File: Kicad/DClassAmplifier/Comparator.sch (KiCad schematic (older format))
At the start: 5 parts

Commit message: Finish off Main Part of Schematic
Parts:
- U? (x3): footprint (none) -> Package_SO:SO-14_3.9x8.65mm_P1.27mm
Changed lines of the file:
@@
 $Descr A4 11693 8268
 encoding utf-8
-Sheet 7 9
+Sheet 3 7
 Title ""
 Date ""
@@
 F 0 "U?" H 5150 3242 50  0000 C CNN
 F 1 "LM319" H 5150 3151 50  0000 C CNN
-F 2 "" H 5150 2875 50  0001 C CNN
+F 2 "Package_SO:SO-14_3.9x8.65mm_P1.27mm" H 5150 2875 50  0001 C CNN
 F 3 "http://www.ti.com/lit/ds/symlink/lm319-n.pdf" H 5150 2875 50  0001 C CNN
 	1    5150 2875
@@
 F 0 "U?" H 5125 3792 50  0000 C CNN
 F 1 "LM319" H 5125 3701 50  0000 C CNN
-F 2 "" H 5125 3425 50  0001 C CNN
+F 2 "Package_SO:SO-14_3.9x8.65mm_P1.27mm" H 5125 3425 50  0001 C CNN
 F 3 "http://www.ti.com/lit/ds/symlink/lm319-n.pdf" H 5125 3425 50  0001 C CNN
 	2    5125 3425
@@
 F 0 "U?" H 5183 4546 50  0000 L CNN
 F 1 "LM319" H 5183 4455 50  0000 L CNN
-F 2 "" H 5225 4500 50  0001 C CNN
+F 2 "Package_SO:SO-14_3.9x8.65mm_P1.27mm" H 5225 4500 50  0001 C CNN
 F 3 "http://www.ti.com/lit/ds/symlink/lm319-n.pdf" H 5225 4500 50  0001 C CNN
 	3    5225 4500

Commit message: updates to schematic
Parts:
- added J2: Conn_01x03, symbol Connector_Generic:Conn_01x03
- R5, R6: renamed from R?; footprint (none) -> Resistor_SMD:R_0603_1608Metric_Pad0.98x0.95mm_HandSolder
- gave numbers to parts that had none: 1
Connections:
- net GND: now also J2.3 (Pin_3)
- net INV_PWM_OUT: now also J2.2 (Pin_2)
- net PWM_OUT: now also J2.1 (Pin_1)
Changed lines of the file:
@@
 $EndDescr
 $Comp
-L Comparator:LM319 U?
+L Comparator:LM319 U1
 U 1 1 61116116
 P 5150 2875
-F 0 "U?" H 5150 3242 50  0000 C CNN
+F 0 "U1" H 5150 3242 50  0000 C CNN
 F 1 "LM319" H 5150 3151 50  0000 C CNN
 F 2 "Package_SO:SO-14_3.9x8.65mm_P1.27mm" H 5150 2875 50  0001 C CNN
@@
 $EndComp
 $Comp
-L Comparator:LM319 U?
+L Comparator:LM319 U1
 U 2 1 6111611C
 P 5125 3425
-F 0 "U?" H 5125 3792 50  0000 C CNN
+F 0 "U1" H 5125 3792 50  0000 C CNN
 F 1 "LM319" H 5125 3701 50  0000 C CNN
 F 2 "Package_SO:SO-14_3.9x8.65mm_P1.27mm" H 5125 3425 50  0001 C CNN
@@
 $EndComp
 $Comp
-L Comparator:LM319 U?
+L Comparator:LM319 U1
 U 3 1 61116122
 P 5225 4500
-F 0 "U?" H 5183 4546 50  0000 L CNN
+F 0 "U1" H 5183 4546 50  0000 L CNN
 F 1 "LM319" H 5183 4455 50  0000 L CNN
 F 2 "Package_SO:SO-14_3.9x8.65mm_P1.27mm" H 5225 4500 50  0001 C CNN
@@
 	1    0    0    -1
 $EndComp
-Wire Wire Line
-	6275 2875 5825 2875
 Wire Wire Line
 	4850 2975 4775 2975
@@
 	4675 3525 4825 3525
 $Comp
-L power:GND #PWR?
+L power:GND #PWR0106
 U 1 1 61116132
 P 5150 3175
-F 0 "#PWR?" H 5150 2925 50  0001 C CNN
+F 0 "#PWR0106" H 5150 2925 50  0001 C CNN
 F 1 "GND" H 5155 3002 50  0000 C CNN
 F 2 "" H 5150 3175 50  0001 C CNN
@@
 $EndComp
 $Comp
-L power:GND #PWR?
+L power:GND #PWR0107
 U 1 1 61116138
 P 5125 3725
-F 0 "#PWR?" H 5125 3475 50  0001 C CNN
+F 0 "#PWR0107" H 5125 3475 50  0001 C CNN
 F 1 "GND" H 5130 3552 50  0000 C CNN
 F 2 "" H 5125 3725 50  0001 C CNN
@@
 $EndComp
 $Comp
-L power:GND #PWR?
+L power:GND #PWR0108
 U 1 1 6111613E
 P 5125 4800
-F 0 "#PWR?" H 5125 4550 50  0001 C CNN
+F 0 "#PWR0108" H 5125 4550 50  0001 C CNN
 F 1 "GND" H 5130 4627 50  0000 C CNN
 F 2 "" H 5125 4800 50  0001 C CNN
@@
 $EndComp
 $Comp
-L power:VCC #PWR?
+L power:VCC #PWR0109
 U 1 1 61116144
 P 5125 4200
-F 0 "#PWR?" H 5125 4050 50  0001 C CNN
+F 0 "#PWR0109" H 5125 4050 50  0001 C CNN
 F 1 "VCC" H 5140 4373 50  0000 C CNN
 F 2 "" H 5125 4200 50  0001 C CNN
@@
 	1    0    0    -1
 $EndComp
-Text HLabel 6275 2875 2    50   Output ~ 0
-PWM_OUT
-Text HLabel 6275 3425 2    50   Output ~ 0
+Text HLabel 7875 3075 2    50   Output ~ 0
 INV_PWM_OUT
 Text HLabel 4350 2975 0    50   Input ~ 0
@@
 	5425 3425 5825 3425
 $Comp
-L Device:R_Small R?
+L Device:R_Small R5
 U 1 1 61119BD5
 P 5825 2700
-F 0 "R?" H 5884 2746 50  0000 L CNN
+F 0 "R5" H 5884 2746 50  0000 L CNN
 F 1 "10k" H 5884 2655 50  0000 L CNN
-F 2 "" H 5825 2700 50  0001 C CNN
+F 2 "Resistor_SMD:R_0603_1608Metric_Pad0.98x0.95mm_HandSolder" H 5825 2700 50  0001 C CNN
 F 3 "~" H 5825 2700 50  0001 C CNN
 	1    5825 2700
@@
 $EndComp
 $Comp
-L Device:R_Small R?
+L Device:R_Small R6
 U 1 1 6111A188
 P 5825 3250
-F 0 "R?" H 5884 3296 50  0000 L CNN
+F 0 "R6" H 5884 3296 50  0000 L CNN
 F 1 "10k" H 5884 3205 50  0000 L CNN
-F 2 "" H 5825 3250 50  0001 C CNN
+F 2 "Resistor_SMD:R_0603_1608Metric_Pad0.98x0.95mm_HandSolder" H 5825 3250 50  0001 C CNN
 F 3 "~" H 5825 3250 50  0001 C CNN
 	1    5825 3250
@@
 $EndComp
 $Comp
-L power:VCC #PWR?
+L power:VCC #PWR0110
 U 1 1 6111A8CA
 P 5825 2500
-F 0 "#PWR?" H 5825 2350 50  0001 C CNN
+F 0 "#PWR0110" H 5825 2350 50  0001 C CNN
 F 1 "VCC" H 5840 2673 50  0000 C CNN
 F 2 "" H 5825 2500 50  0001 C CNN
@@
 $EndComp
 $Comp
-L power:VCC #PWR?
+L power:VCC #PWR0111
 U 1 1 6111AE94
 P 5825 3100
-F 0 "#PWR?" H 5825 2950 50  0001 C CNN
+F 0 "#PWR0111" H 5825 2950 50  0001 C CNN
 F 1 "VCC" H 5840 3273 50  0000 C CNN
 F 2 "" H 5825 3100 50  0001 C CNN
@@
 Wire Wire Line
 	5825 2875 5825 2800
-Connection ~ 5825 2875
 Wire Wire Line
 	5825 2875 5450 2875
@@
 	4775 2975 4350 2975
 Connection ~ 4775 2975
+$Comp
+L Connector_Generic:Conn_01x03 J2
+U 1 1 611080B2
+P 7675 3075
+F 0 "J2" H 7755 3117 50  0000 L CNN
+F 1 "Conn_01x03" H 7755 3026 50  0000 L CNN
+F 2 "" H 7675 3075 50  0001 C CNN
+F 3 "~" H 7675 3075 50  0001 C CNN
+	1    7675 3075
+	-1   0    0    -1
+$EndComp
+Text HLabel 7875 2975 2    50   Output ~ 0
+PWM_OUT
+Connection ~ 5825 2875
+Wire Wire Line
+	6275 2875 5825 2875
+$Comp
+L power:GND #PWR0112
+U 1 1 6110885B
+P 7875 3175
+F 0 "#PWR0112" H 7875 2925 50  0001 C CNN
+F 1 "GND" H 7880 3002 50  0000 C CNN
+F 2 "" H 7875 3175 50  0001 C CNN
+F 3 "" H 7875 3175 50  0001 C CNN
+	1    7875 3175
+	-1   0    0    -1
+$EndComp
+Text Label 7875 2975 0    50   ~ 0
+PWM_OUT
+Text Label 7875 3075 0    50   ~ 0
+INV_PWM_OUT
+Text Label 6275 2875 0    50   ~ 0
+PWM_OUT
+Text Label 6275 3425 0    50   ~ 0
+INV_PWM_OUT
 $EndSCHEMATC

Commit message: Added footprints to schematic
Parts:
- J2: footprint (none) -> Connector_PinSocket_2.54mm:PinSocket_1x03_P2.54mm_Vertical
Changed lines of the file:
@@
 F 0 "J2" H 7755 3117 50  0000 L CNN
 F 1 "Conn_01x03" H 7755 3026 50  0000 L CNN
-F 2 "" H 7675 3075 50  0001 C CNN
+F 2 "Connector_PinSocket_2.54mm:PinSocket_1x03_P2.54mm_Vertical" H 7675 3075 50  0001 C CNN
 F 3 "~" H 7675 3075 50  0001 C CNN
 	1    7675 3075

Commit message: Update Terminal Block Footprints
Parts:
- J2: footprint Connector_PinSocket_2.54mm:PinSocket_1x03_P2.54mm_Vertical -> TerminalBlock:TerminalBlock_bornier-3_P5.08mm
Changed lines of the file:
@@
 F 0 "J2" H 7755 3117 50  0000 L CNN
 F 1 "Conn_01x03" H 7755 3026 50  0000 L CNN
-F 2 "Connector_PinSocket_2.54mm:PinSocket_1x03_P2.54mm_Vertical" H 7675 3075 50  0001 C CNN
+F 2 "TerminalBlock:TerminalBlock_bornier-3_P5.08mm" H 7675 3075 50  0001 C CNN
 F 3 "~" H 7675 3075 50  0001 C CNN
 	1    7675 3075

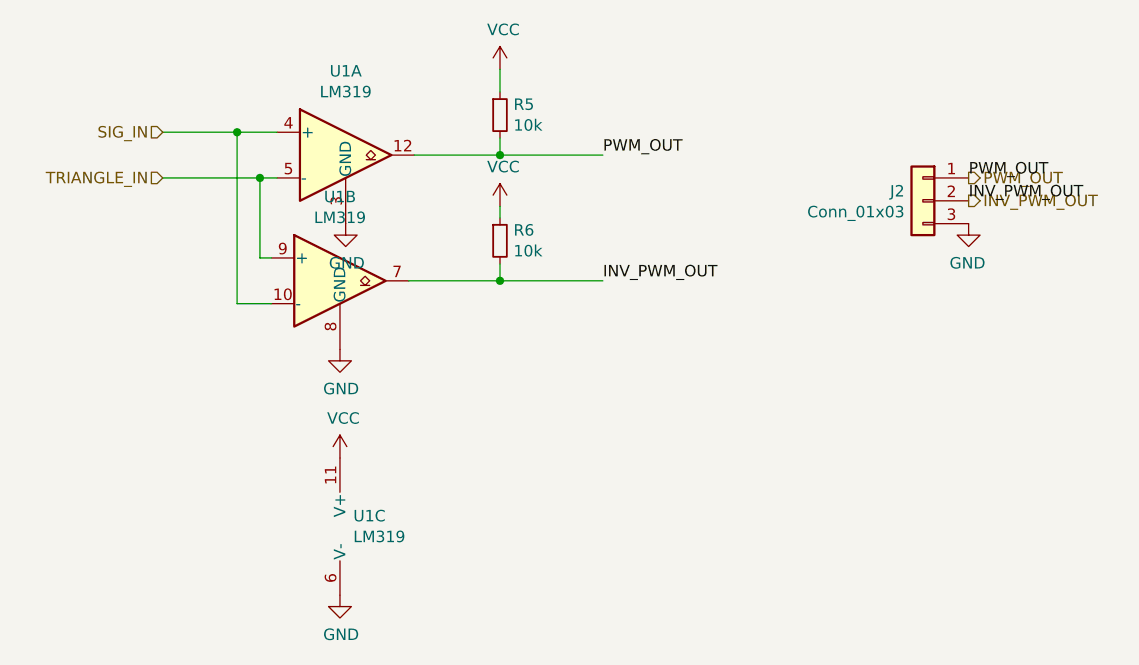
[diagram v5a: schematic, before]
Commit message: Add Test Points
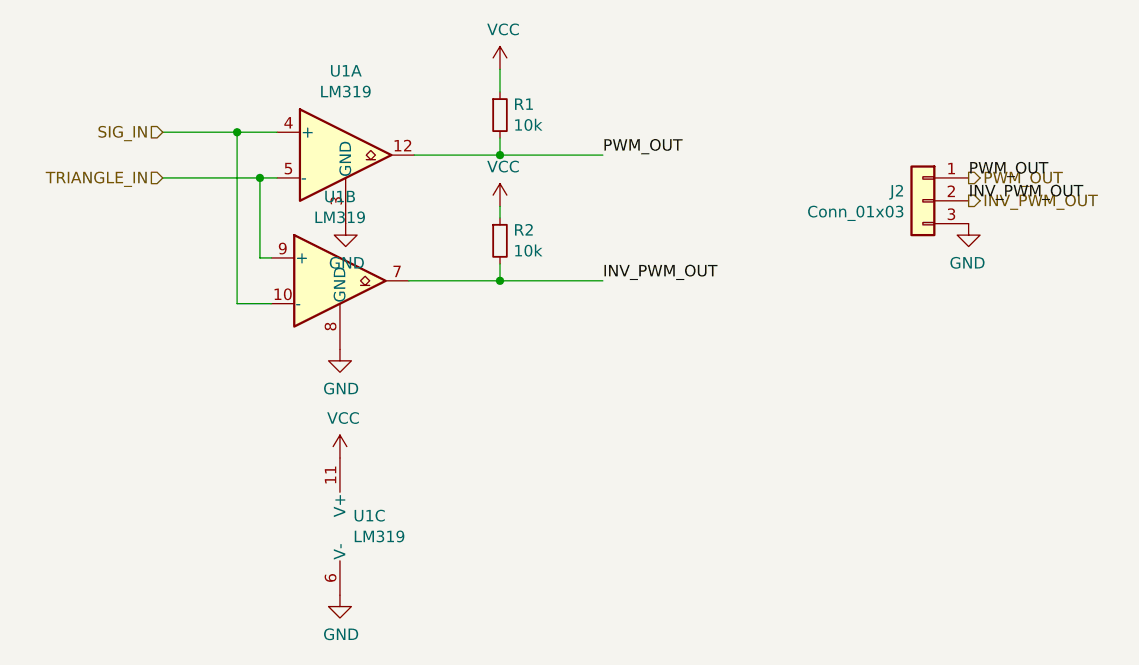
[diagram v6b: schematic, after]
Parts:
- renumbered R5 to R1, R6 to R2
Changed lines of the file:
@@
 	4675 3525 4825 3525
 $Comp
-L power:GND #PWR0106
+L power:GND #PWR010
 U 1 1 61116132
 P 5150 3175
-F 0 "#PWR0106" H 5150 2925 50  0001 C CNN
+F 0 "#PWR010" H 5150 2925 50  0001 C CNN
 F 1 "GND" H 5155 3002 50  0000 C CNN
 F 2 "" H 5150 3175 50  0001 C CNN
@@
 $EndComp
 $Comp
-L power:GND #PWR0107
+L power:GND #PWR07
 U 1 1 61116138
 P 5125 3725
-F 0 "#PWR0107" H 5125 3475 50  0001 C CNN
+F 0 "#PWR07" H 5125 3475 50  0001 C CNN
 F 1 "GND" H 5130 3552 50  0000 C CNN
 F 2 "" H 5125 3725 50  0001 C CNN
@@
 $EndComp
 $Comp
-L power:GND #PWR0108
+L power:GND #PWR09
 U 1 1 6111613E
 P 5125 4800
-F 0 "#PWR0108" H 5125 4550 50  0001 C CNN
+F 0 "#PWR09" H 5125 4550 50  0001 C CNN
 F 1 "GND" H 5130 4627 50  0000 C CNN
 F 2 "" H 5125 4800 50  0001 C CNN
@@
 $EndComp
 $Comp
-L power:VCC #PWR0109
+L power:VCC #PWR08
 U 1 1 61116144
 P 5125 4200
-F 0 "#PWR0109" H 5125 4050 50  0001 C CNN
+F 0 "#PWR08" H 5125 4050 50  0001 C CNN
 F 1 "VCC" H 5140 4373 50  0000 C CNN
 F 2 "" H 5125 4200 50  0001 C CNN
@@
 	5425 3425 5825 3425
 $Comp
-L Device:R_Small R5
+L Device:R_Small R1
 U 1 1 61119BD5
 P 5825 2700
-F 0 "R5" H 5884 2746 50  0000 L CNN
+F 0 "R1" H 5884 2746 50  0000 L CNN
 F 1 "10k" H 5884 2655 50  0000 L CNN
 F 2 "Resistor_SMD:R_0603_1608Metric_Pad0.98x0.95mm_HandSolder" H 5825 2700 50  0001 C CNN
@@
 $EndComp
 $Comp
-L Device:R_Small R6
+L Device:R_Small R2
 U 1 1 6111A188
 P 5825 3250
-F 0 "R6" H 5884 3296 50  0000 L CNN
+F 0 "R2" H 5884 3296 50  0000 L CNN
 F 1 "10k" H 5884 3205 50  0000 L CNN
 F 2 "Resistor_SMD:R_0603_1608Metric_Pad0.98x0.95mm_HandSolder" H 5825 3250 50  0001 C CNN
@@
 $EndComp
 $Comp
-L power:VCC #PWR0110
+L power:VCC #PWR011
 U 1 1 6111A8CA
 P 5825 2500
-F 0 "#PWR0110" H 5825 2350 50  0001 C CNN
+F 0 "#PWR011" H 5825 2350 50  0001 C CNN
 F 1 "VCC" H 5840 2673 50  0000 C CNN
 F 2 "" H 5825 2500 50  0001 C CNN
@@
 $EndComp
 $Comp
-L power:VCC #PWR0111
+L power:VCC #PWR012
 U 1 1 6111AE94
 P 5825 3100
-F 0 "#PWR0111" H 5825 2950 50  0001 C CNN
+F 0 "#PWR012" H 5825 2950 50  0001 C CNN
 F 1 "VCC" H 5840 3273 50  0000 C CNN
 F 2 "" H 5825 3100 50  0001 C CNN
@@
 	6275 2875 5825 2875
 $Comp
-L power:GND #PWR0112
+L power:GND #PWR013
 U 1 1 6110885B
 P 7875 3175
-F 0 "#PWR0112" H 7875 2925 50  0001 C CNN
+F 0 "#PWR013" H 7875 2925 50  0001 C CNN
 F 1 "GND" H 7880 3002 50  0000 C CNN
 F 2 "" H 7875 3175 50  0001 C CNN

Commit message: PCB for input and added filter caps
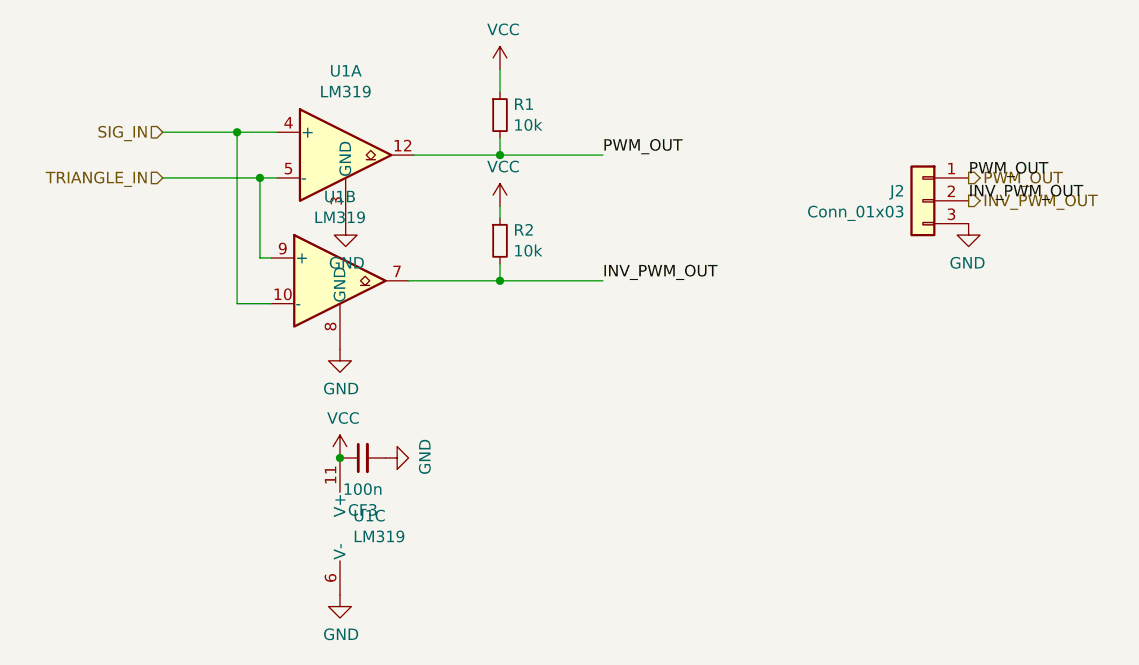
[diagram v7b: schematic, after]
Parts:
- added CF3: 100n, Capacitor_SMD:C_0805_2012Metric_Pad1.18x1.45mm_HandSolder, symbol Device:C_Small
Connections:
- net GND: now also CF3.2
- net VCC: now also CF3.1
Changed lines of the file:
@@
 $Descr A4 11693 8268
 encoding utf-8
-Sheet 3 6
+Sheet 5 6
 Title ""
 Date ""
@@
 Text Label 6275 3425 0    50   ~ 0
 INV_PWM_OUT
+$Comp
+L Device:C_Small CF?
+U 1 1 611DC342
+P 5225 4200
+AR Path="/610C616D/611DC342" Ref="CF?"  Part="1"
+AR Path="/611D4178/611DC342" Ref="CF?"  Part="1"
+AR Path="/61113C55/611DC342" Ref="CF3"  Part="1"
+F 0 "CF3" V 4996 4200 50  0000 C CNN
+F 1 "100n" V 5087 4200 50  0000 C CNN
+F 2 "Capacitor_SMD:C_0805_2012Metric_Pad1.18x1.45mm_HandSolder" H 5225 4200 50  0001 C CNN
+F 3 "~" H 5225 4200 50  0001 C CNN
+	1    5225 4200
+	0    -1   -1   0
+$EndComp
+$Comp
+L power:GND #PWR?
+U 1 1 611DC348
+P 5325 4200
+F 0 "#PWR?" H 5325 3950 50  0001 C CNN
+F 1 "GND" H 5330 4027 50  0000 C CNN
+F 2 "" H 5325 4200 50  0001 C CNN
+F 3 "" H 5325 4200 50  0001 C CNN
+	1    5325 4200
+	0    -1   -1   0
+$EndComp
+Connection ~ 5125 4200
 $EndSCHEMATC

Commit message: Combined Board
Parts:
- removed J2: Conn_01x03, TerminalBlock:TerminalBlock_bornier-3_P5.08mm, symbol Connector_Generic:Conn_01x03
- C15: renamed from CF3; footprint Capacitor_SMD:C_0805_2012Metric_Pad1.18x1.45mm_HandSolder -> Capacitor_SMD:C_0603_1608Metric_Pad1.08x0.95mm_HandSolder
- renumbered R1 to R26, R2 to R27, U1 to U5
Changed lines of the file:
@@
 $EndDescr
 $Comp
-L Comparator:LM319 U1
+L Comparator:LM319 U5
 U 1 1 61116116
 P 5150 2875
-F 0 "U1" H 5150 3242 50  0000 C CNN
+F 0 "U5" H 5150 3242 50  0000 C CNN
 F 1 "LM319" H 5150 3151 50  0000 C CNN
 F 2 "Package_SO:SO-14_3.9x8.65mm_P1.27mm" H 5150 2875 50  0001 C CNN
@@
 $EndComp
 $Comp
-L Comparator:LM319 U1
+L Comparator:LM319 U5
 U 2 1 6111611C
 P 5125 3425
-F 0 "U1" H 5125 3792 50  0000 C CNN
+F 0 "U5" H 5125 3792 50  0000 C CNN
 F 1 "LM319" H 5125 3701 50  0000 C CNN
 F 2 "Package_SO:SO-14_3.9x8.65mm_P1.27mm" H 5125 3425 50  0001 C CNN
@@
 $EndComp
 $Comp
-L Comparator:LM319 U1
+L Comparator:LM319 U5
 U 3 1 61116122
 P 5225 4500
-F 0 "U1" H 5183 4546 50  0000 L CNN
+F 0 "U5" H 5183 4546 50  0000 L CNN
 F 1 "LM319" H 5183 4455 50  0000 L CNN
 F 2 "Package_SO:SO-14_3.9x8.65mm_P1.27mm" H 5225 4500 50  0001 C CNN
@@
 	4675 3525 4825 3525
 $Comp
-L power:GND #PWR010
+L power:GND #PWR044
 U 1 1 61116132
 P 5150 3175
-F 0 "#PWR010" H 5150 2925 50  0001 C CNN
+F 0 "#PWR044" H 5150 2925 50  0001 C CNN
 F 1 "GND" H 5155 3002 50  0000 C CNN
 F 2 "" H 5150 3175 50  0001 C CNN
@@
 $EndComp
 $Comp
-L power:GND #PWR07
+L power:GND #PWR045
 U 1 1 61116138
 P 5125 3725
-F 0 "#PWR07" H 5125 3475 50  0001 C CNN
+F 0 "#PWR045" H 5125 3475 50  0001 C CNN
 F 1 "GND" H 5130 3552 50  0000 C CNN
 F 2 "" H 5125 3725 50  0001 C CNN
@@
 $EndComp
 $Comp
-L power:GND #PWR09
+L power:GND #PWR048
 U 1 1 6111613E
 P 5125 4800
-F 0 "#PWR09" H 5125 4550 50  0001 C CNN
+F 0 "#PWR048" H 5125 4550 50  0001 C CNN
 F 1 "GND" H 5130 4627 50  0000 C CNN
 F 2 "" H 5125 4800 50  0001 C CNN
@@
 $EndComp
 $Comp
-L power:VCC #PWR08
+L power:VCC #PWR046
 U 1 1 61116144
 P 5125 4200
-F 0 "#PWR08" H 5125 4050 50  0001 C CNN
+F 0 "#PWR046" H 5125 4050 50  0001 C CNN
 F 1 "VCC" H 5140 4373 50  0000 C CNN
 F 2 "" H 5125 4200 50  0001 C CNN
@@
 	1    0    0    -1
 $EndComp
-Text HLabel 7875 3075 2    50   Output ~ 0
-INV_PWM_OUT
 Text HLabel 4350 2975 0    50   Input ~ 0
 TRIANGLE_IN
@@
 	5425 3425 5825 3425
 $Comp
-L Device:R_Small R1
+L Device:R_Small R26
 U 1 1 61119BD5
 P 5825 2700
-F 0 "R1" H 5884 2746 50  0000 L CNN
+F 0 "R26" H 5884 2746 50  0000 L CNN
 F 1 "10k" H 5884 2655 50  0000 L CNN
 F 2 "Resistor_SMD:R_0603_1608Metric_Pad0.98x0.95mm_HandSolder" H 5825 2700 50  0001 C CNN
@@
 $EndComp
 $Comp
-L Device:R_Small R2
+L Device:R_Small R27
 U 1 1 6111A188
 P 5825 3250
-F 0 "R2" H 5884 3296 50  0000 L CNN
+F 0 "R27" H 5884 3296 50  0000 L CNN
 F 1 "10k" H 5884 3205 50  0000 L CNN
 F 2 "Resistor_SMD:R_0603_1608Metric_Pad0.98x0.95mm_HandSolder" H 5825 3250 50  0001 C CNN
@@
 $EndComp
 $Comp
-L power:VCC #PWR011
+L power:VCC #PWR042
 U 1 1 6111A8CA
 P 5825 2500
-F 0 "#PWR011" H 5825 2350 50  0001 C CNN
+F 0 "#PWR042" H 5825 2350 50  0001 C CNN
 F 1 "VCC" H 5840 2673 50  0000 C CNN
 F 2 "" H 5825 2500 50  0001 C CNN
@@
 $EndComp
 $Comp
-L power:VCC #PWR012
+L power:VCC #PWR043
 U 1 1 6111AE94
 P 5825 3100
-F 0 "#PWR012" H 5825 2950 50  0001 C CNN
+F 0 "#PWR043" H 5825 2950 50  0001 C CNN
 F 1 "VCC" H 5840 3273 50  0000 C CNN
 F 2 "" H 5825 3100 50  0001 C CNN
@@
 	4775 2975 4350 2975
 Connection ~ 4775 2975
-$Comp
-L Connector_Generic:Conn_01x03 J2
-U 1 1 611080B2
-P 7675 3075
-F 0 "J2" H 7755 3117 50  0000 L CNN
-F 1 "Conn_01x03" H 7755 3026 50  0000 L CNN
-F 2 "TerminalBlock:TerminalBlock_bornier-3_P5.08mm" H 7675 3075 50  0001 C CNN
-F 3 "~" H 7675 3075 50  0001 C CNN
-	1    7675 3075
-	-1   0    0    -1
-$EndComp
-Text HLabel 7875 2975 2    50   Output ~ 0
-PWM_OUT
 Connection ~ 5825 2875
 Wire Wire Line
 	6275 2875 5825 2875
 $Comp
-L power:GND #PWR013
-U 1 1 6110885B
-P 7875 3175
-F 0 "#PWR013" H 7875 2925 50  0001 C CNN
-F 1 "GND" H 7880 3002 50  0000 C CNN
-F 2 "" H 7875 3175 50  0001 C CNN
-F 3 "" H 7875 3175 50  0001 C CNN
-	1    7875 3175
-	-1   0    0    -1
-$EndComp
-Text Label 7875 2975 0    50   ~ 0
-PWM_OUT
-Text Label 7875 3075 0    50   ~ 0
-INV_PWM_OUT
-Text Label 6275 2875 0    50   ~ 0
-PWM_OUT
-Text Label 6275 3425 0    50   ~ 0
-INV_PWM_OUT
-$Comp
-L Device:C_Small CF?
+L Device:C_Small C?
 U 1 1 611DC342
 P 5225 4200
-AR Path="/610C616D/611DC342" Ref="CF?"  Part="1"
-AR Path="/611D4178/611DC342" Ref="CF?"  Part="1"
-AR Path="/61113C55/611DC342" Ref="CF3"  Part="1"
-F 0 "CF3" V 4996 4200 50  0000 C CNN
+AR Path="/610C616D/611DC342" Ref="C?"  Part="1"
+AR Path="/611D4178/611DC342" Ref="C?"  Part="1"
+AR Path="/61113C55/611DC342" Ref="C15"  Part="1"
+F 0 "C15" V 4996 4200 50  0000 C CNN
 F 1 "100n" V 5087 4200 50  0000 C CNN
-F 2 "Capacitor_SMD:C_0805_2012Metric_Pad1.18x1.45mm_HandSolder" H 5225 4200 50  0001 C CNN
+F 2 "Capacitor_SMD:C_0603_1608Metric_Pad1.08x0.95mm_HandSolder" H 5225 4200 50  0001 C CNN
 F 3 "~" H 5225 4200 50  0001 C CNN
 	1    5225 4200
@@
 $EndComp
 $Comp
-L power:GND #PWR?
+L power:GND #PWR047
 U 1 1 611DC348
 P 5325 4200
-F 0 "#PWR?" H 5325 3950 50  0001 C CNN
+F 0 "#PWR047" H 5325 3950 50  0001 C CNN
 F 1 "GND" H 5330 4027 50  0000 C CNN
 F 2 "" H 5325 4200 50  0001 C CNN
@@
 $EndComp
 Connection ~ 5125 4200
+Text HLabel 6275 3425 2    50   Output ~ 0
+INV_PWM_OUT
+Text HLabel 6275 2875 2    50   Output ~ 0
+PWM_OUT
 $EndSCHEMATC
